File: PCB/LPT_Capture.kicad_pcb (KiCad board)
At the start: 2 copper layers, 36 x 20.8 mm, 12 parts, among them J1 USB3155-XX-X_REVA, J2 DB25 Male, U1 FT245RL

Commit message: minor routing straighten
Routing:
- net /~{TXE}: track 23.6 -> 22.9 mm
- net VCC: track 36.3 -> 35.7 mm
- net GND: vias 16 -> 15
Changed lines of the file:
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@@
   (title_block
     (title "LPT_Capture")
-    (date "2023-09-11")
-    (rev "011")
+    (date "2023-09-12")
+    (rev "012")
     (company "b.kenyon.w@gmail.com")
     (comment 1 "CC-BY-SA")
@@
     (pad "25" smd roundrect (at 15.235 -0.5 180) (size 2 4.6) (layers "B.Cu" "B.Mask") (roundrect_rratio 0.25)
       (net 1 "GND") (pinfunction "P25") (pintype "passive"))
-    (model "${KIPRJMOD}/000_LOCAL.pretty/3d/956-025-010R0.STEP"
+    (model "${KIPRJMOD}/000_LOCAL.pretty/3d/956-025-010R0.STEP" hide
       (offset (xyz 0 -9.85 -9.4))
       (scale (xyz 1 1 1))
@@
   (via (at 166.8 107.15) (size 0.5) (drill 0.3) (layers "F.Cu" "B.Cu") (free) (net 1))
   (via (at 154.7 102) (size 0.5) (drill 0.3) (layers "F.Cu" "B.Cu") (free) (net 1))
-  (via (at 144.5 102.7) (size 0.5) (drill 0.3) (layers "F.Cu" "B.Cu") (free) (net 1))
   (via (at 162.65 103.75) (size 0.5) (drill 0.3) (layers "F.Cu" "B.Cu") (net 1))
   (via (at 152.05 105.5) (size 0.5) (drill 0.3) (layers "F.Cu" "B.Cu") (free) (net 1))
@@
   (segment (start 160.5 107.25) (end 160.5 99.8) (width 0.2) (layer "F.Cu") (net 11))
   (segment (start 162.35 109.1) (end 160.5 107.25) (width 0.2) (layer "F.Cu") (net 11))
-  (segment (start 143.6 97.9) (end 142.85 97.9) (width 0.2) (layer "F.Cu") (net 12))
   (segment (start 162.9 105.225) (end 164.8 105.225) (width 0.2) (layer "F.Cu") (net 12))
+  (segment (start 142.85 98.75) (end 142.85 97.9) (width 0.2) (layer "F.Cu") (net 12))
   (via (at 162.9 105.225) (size 0.5) (drill 0.3) (layers "F.Cu" "B.Cu") (net 12))
-  (via (at 143.6 97.9) (size 0.5) (drill 0.3) (layers "F.Cu" "B.Cu") (net 12))
-  (segment (start 160.275 102.6) (end 148.3 102.6) (width 0.2) (layer "B.Cu") (net 12))
-  (segment (start 148.3 102.6) (end 143.6 97.9) (width 0.2) (layer "B.Cu") (net 12))
-  (segment (start 162.9 105.225) (end 160.275 102.6) (width 0.2) (layer "B.Cu") (net 12))
+  (via (at 142.85 98.75) (size 0.5) (drill 0.3) (layers "F.Cu" "B.Cu") (net 12))
+  (segment (start 160.275 102.6) (end 162.9 105.225) (width 0.2) (layer "B.Cu") (net 12))
+  (segment (start 142.85 98.75) (end 146.7 102.6) (width 0.2) (layer "B.Cu") (net 12))
+  (segment (start 146.7 102.6) (end 160.275 102.6) (width 0.2) (layer "B.Cu") (net 12))
   (segment (start 162.8 98.05) (end 162.8 97.9) (width 0.2) (layer "F.Cu") (net 13))
   (segment (start 163.55 98.8) (end 162.8 98.05) (width 0.2) (layer "F.Cu") (net 13))
@@
   (via (at 140.45 98.75) (size 0.5) (drill 0.3) (layers "F.Cu" "B.Cu") (net 14))
   (via (at 158.85 104.575) (size 0.5) (drill 0.3) (layers "F.Cu" "B.Cu") (net 14))
-  (segment (start 147.45 103.6) (end 147.45 102.45) (width 0.2) (layer "B.Cu") (net 14))
+  (segment (start 145.65 103.95) (end 140.45 98.75) (width 0.2) (layer "B.Cu") (net 14))
   (segment (start 158.85 104.575) (end 158.225 103.95) (width 0.2) (layer "B.Cu") (net 14))
-  (segment (start 158.225 103.95) (end 147.8 103.95) (width 0.2) (layer "B.Cu") (net 14))
-  (segment (start 147.45 102.45) (end 143.75 98.75) (width 0.2) (layer "B.Cu") (net 14))
-  (segment (start 143.75 98.75) (end 140.45 98.75) (width 0.2) (layer "B.Cu") (net 14))
-  (segment (start 147.8 103.95) (end 147.45 103.6) (width 0.2) (layer "B.Cu") (net 14))
+  (segment (start 158.225 103.95) (end 145.65 103.95) (width 0.2) (layer "B.Cu") (net 14))
   (segment (start 164.925 106.4) (end 165.9 106.4) (width 0.2) (layer "F.Cu") (net 15))
   (segment (start 155.65 105) (end 155.65 103) (width 0.6) (layer "F.Cu") (net 15))
@@
   (via (at 148.1 103.3) (size 0.5) (drill 0.3) (layers "F.Cu" "B.Cu") (net 15))
   (via (at 162.9 106.525) (size 0.5) (drill 0.3) (layers "F.Cu" "B.Cu") (net 15))
-  (segment (start 160.65 104) (end 160.65 105.05) (width 0.6) (layer "B.Cu") (net 15))
+  (segment (start 148.1 103.3) (end 158.9 103.3) (width 0.6) (layer "B.Cu") (net 15))
   (segment (start 162.125 106.525) (end 162.9 106.525) (width 0.6) (layer "B.Cu") (net 15))
-  (segment (start 159.95 103.3) (end 160.65 104) (width 0.6) (layer "B.Cu") (net 15))
-  (segment (start 160.65 105.05) (end 162.125 106.525) (width 0.6) (layer "B.Cu") (net 15))
-  (segment (start 148.1 103.3) (end 159.95 103.3) (width 0.6) (layer "B.Cu") (net 15))
+  (segment (start 158.9 103.3) (end 162.125 106.525) (width 0.6) (layer "B.Cu") (net 15))
   (segment (start 162.465 92.55) (end 159.695 92.55) (width 0.2) (layer "B.Cu") (net 16))
   (segment (start 142.85 96.1) (end 142.85 96) (width 0.2) (layer "F.Cu") (net 17))

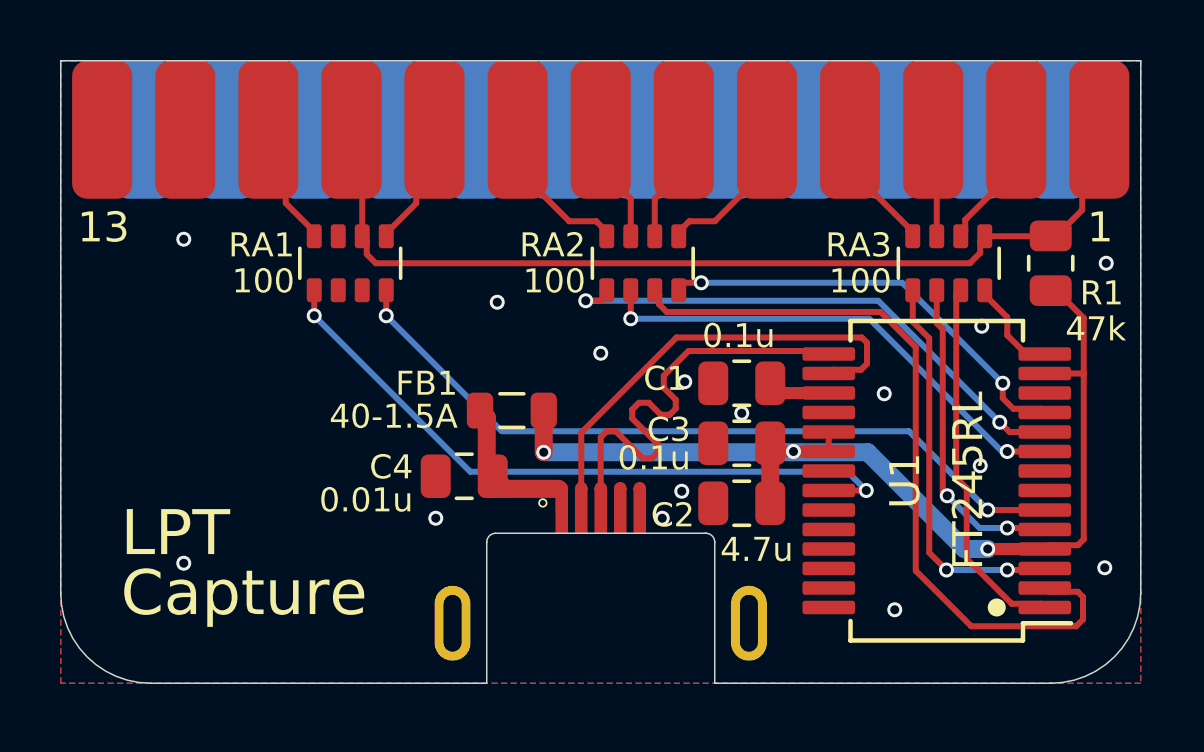
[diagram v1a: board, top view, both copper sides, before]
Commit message: add ONLINE & /RESET
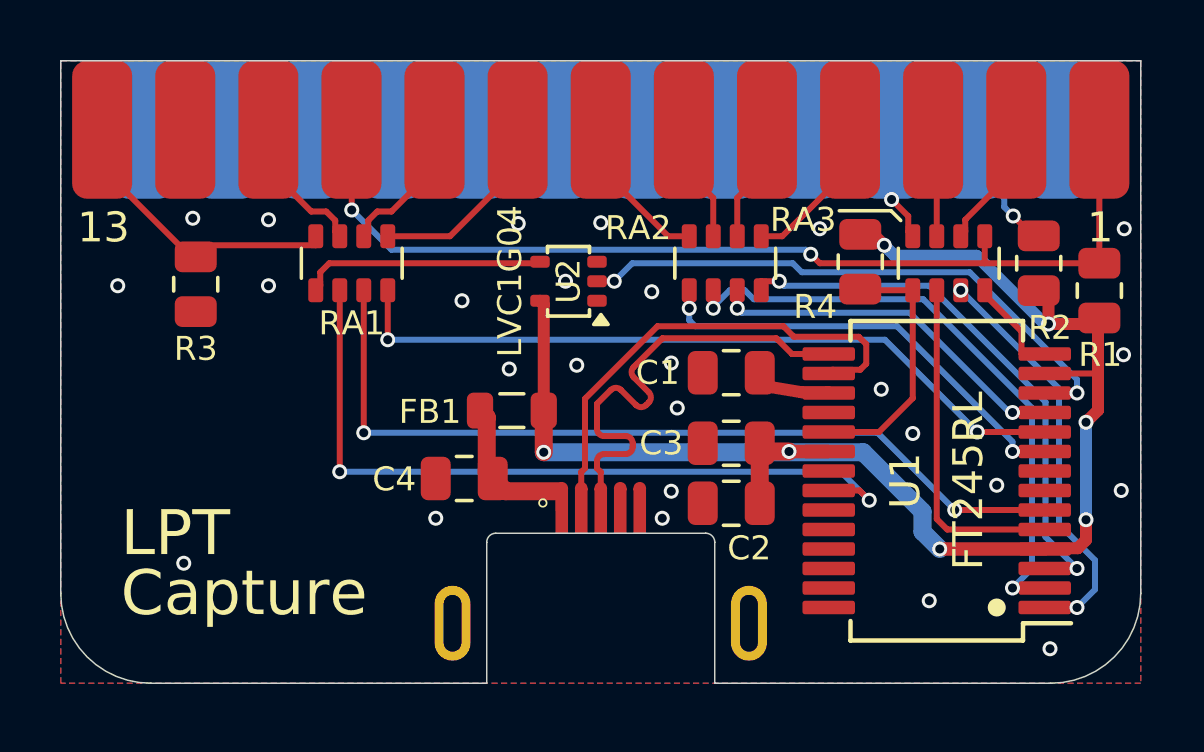
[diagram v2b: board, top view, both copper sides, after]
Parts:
- added R2: 47k, 000_LOCAL:R_0805_2012Metric, F.Cu at (164.6, 97.0)
- added R3: 47k, 000_LOCAL:R_0805_2012Metric, F.Cu at (136.5, 97.7)
- added R4: 47k, 000_LOCAL:R_0805_2012Metric, F.Cu at (158.7, 97.0)
- added U2: LVC1G04, 000_LOCAL:SOT-353_SC-70-5, F.Cu at (148.9, 97.6)
- C4: value 0.01u -> 10n
- moved RA2 2.75 mm to (154.2, 97.0)
- moved R1 1.86 mm to (166.6, 97.9)
- moved C1 0.49 mm to (154.3, 100.7)
- moved C2 0.35 mm to (154.3, 105.0)
- moved C3 0.35 mm to (154.3, 103.0)
- moved C4 0.08 mm to (145.4, 104.2)
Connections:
- net /PD0 renamed /pD0
- net /PD1 renamed /pD1
- net /~{AutoLineFeed} renamed /~{pAUTOF}
- net /~{Select-Printer} renamed /~{pSELECT}
- J2 pad 1: /~{STROBE} -> /~{pSTROBE}
- J2 pad 10: /~{STROBE} -> /~{pSTROBE}
- J2 pad 11: /BUSY -> /pBUSY
- J2 pad 13: /Select -> /pONLINE
- J2 pad 15: /RST_ERR -> /~{pERROR}
- J2 pad 16: /RST_ERR -> /~{pRESET}
- J2 pad 4: /PD2 -> /pD2
- J2 pad 5: /PD3 -> /pD3
- J2 pad 6: /PD4 -> /pD4
- J2 pad 7: /PD5 -> /pD5
- J2 pad 8: /PD6 -> /pD6
- J2 pad 9: /PD7 -> /pD7
- R1 pad 1: /~{STROBE} -> /~{pSTROBE}
- RA1 pad 1: /~{TXE} -> /PWREN
- RA1 pad 2: GND -> /~{TXE}
- RA1 pad 3: unconnected-(RA1-R3.1-Pad3) -> /D7
- RA1 pad 4: /D7 -> /D6
- RA1 pad 5: /PD7 -> /pD6
- RA1 pad 6: /~{STROBE} -> /pD7
- RA1 pad 7: GND -> /pBUSY
- RA1 pad 8: /BUSY -> /pONLINE
- RA2 pad 1: /D6 -> /D5
- RA2 pad 2: /D5 -> /D4
- RA2 pad 3: /D4 -> /D3
- RA2 pad 4: /D3 -> /D2
- RA2 pad 5: /PD3 -> /pD2
- RA2 pad 6: /PD4 -> /pD3
- RA2 pad 7: /PD5 -> /pD4
- RA2 pad 8: /PD6 -> /pD5
- RA3 pad 1: /D2 -> /~{RESET}
- RA3 pad 5: /~{STROBE} -> /~{pSTROBE}
- RA3 pad 8: /PD2 -> /~{pRESET}
- U1 pad 12: unconnected-(U1-~{PWREN}-Pad12) -> /~{PWREN}
- U1 pad 19: VCC -> /~{RESET}
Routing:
- net /~{pSTROBE}: track 0.00 -> 33.7 mm, vias 0 -> 2
- net /~{STROBE}: track 32.2 -> 0.00 mm
- net /~{PWREN}: track 0.00 -> 19.4 mm, vias 0 -> 2
- net VCC: track 35.7 -> 49.3 mm, vias 3 -> 7
- net /pONLINE: track 0.00 -> 9.76 mm
- net /~{RESET}: track 0.00 -> 8.49 mm
- net /PWREN: track 0.00 -> 8.13 mm
- net /D6: track 18.0 -> 24.8 mm
- net /pD6: track 0.00 -> 6.56 mm
- net /D2: track 13.1 -> 18.5 mm
- net /PD6: track 5.31 -> 0.00 mm
- net /PD3: track 5.27 -> 0.00 mm
- net /D4: track 25.7 -> 20.5 mm, vias 0 -> 2
- net /pD2: track 0.00 -> 5.19 mm
- net /pD5: track 0.00 -> 5.18 mm
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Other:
- board text added: "R1-R4 ${00000000-0000-0000-0000-000060bbe2fe:VALUE} RA1-RA3 ${00000000-0000-0000-0000-000060bbe78d:VALUE} C1,C3 ${00000000-0000-0000-0000-000060bbeb15:VALUE} C2 ${00000000-0000-0000-0000-000060bbe5e0:VALUE} C4 ${00000000-0000-0000-0000-000060cac7fa:VALUE} FB1 ${00000000-0000-0000-0000-000060ca1001:VALUE}"

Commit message: pfet invert for online, bom
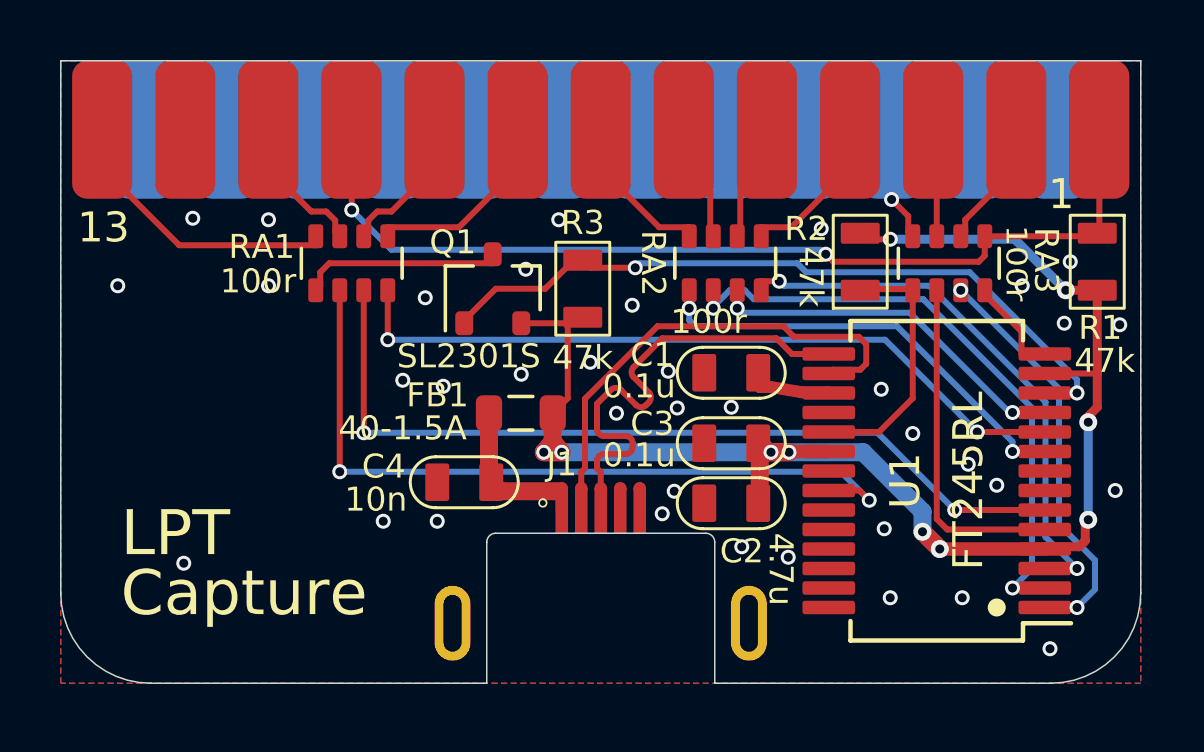
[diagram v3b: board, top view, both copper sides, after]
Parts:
- removed the R2 at (164.6, 97.0)
- removed U2: LVC1G04, 000_LOCAL:SOT-353_SC-70-5
- added N1: Housing, 000_LOCAL:DSUB-25_Housing, F.Cu at (150.0, 92.5)
- added Q1: SL2301S, 000_LOCAL:SOT-23, F.Cu at (146.4, 97.8)
- C1, C2, C3, C4: footprint 000_LOCAL:C_0805_2012Metric -> 000_LOCAL:C_0805
- J1: value USB3155-XX-X_REVA -> USB3155-XX-X; footprint 000_LOCAL:GCT_USB3155-XX-X_REVA -> 000_LOCAL:GCT_USB3155-XX-X
- R1, R3: footprint 000_LOCAL:R_0805_2012Metric -> 000_LOCAL:R_0805
- R2: renamed from R4; footprint 000_LOCAL:R_0805_2012Metric -> 000_LOCAL:R_0805
- RA1, RA2, RA3: value 100 -> 100r
- moved R3 12.9 mm to (149.4, 97.8), turned to -90 degrees
- moved J2 1.90 mm to (150.0, 90.2)
- moved R1 0.97 mm to (166.6, 97.0)
- moved FB1 0.31 mm to (147.3, 102.0)
- moved C4 0.12 mm to (145.4, 104.3)
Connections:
- R3 pad 1: GND -> /~{PWREN}
- R3 pad 2: /pONLINE -> VCC
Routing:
- net /~{PWREN}: track 19.4 -> 24.6 mm
- net /~{pERROR}: track 4.53 -> 0.00 mm, vias 1 -> 0
- net /~{pRESET}: track 1.52 -> 3.84 mm
- net VCC: track 49.3 -> 51.0 mm, vias 7 -> 10
- net /PWREN: track 8.13 -> 6.84 mm
- net /~{pSTROBE}: track 33.7 -> 32.5 mm
- net GND: vias 26 -> 37
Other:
- board text added: "J1: ${00000000-0000-0000-0000-000060db353c:VALUE}"
- board text added: "PCB THICKNESS 1.2mm"
- board text removed: "R1-R4 ${00000000-0000-0000-0000-000060bbe2fe:VALUE} RA1-RA3 ${00000000-0000-0000-0000-000060bbe78d:VALUE} C1,C3 ${00000000-0000-0000-0000-000060bbeb15:VALUE} C2 ${00000000-0000-0000-0000-000060bbe5e0:VALUE} C4 ${00000000-0000-0000-0000-000060cac7fa:VALUE} FB1 ${00000000-0000-0000-0000-000060ca1001:VALUE}"

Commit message: add /SELECT
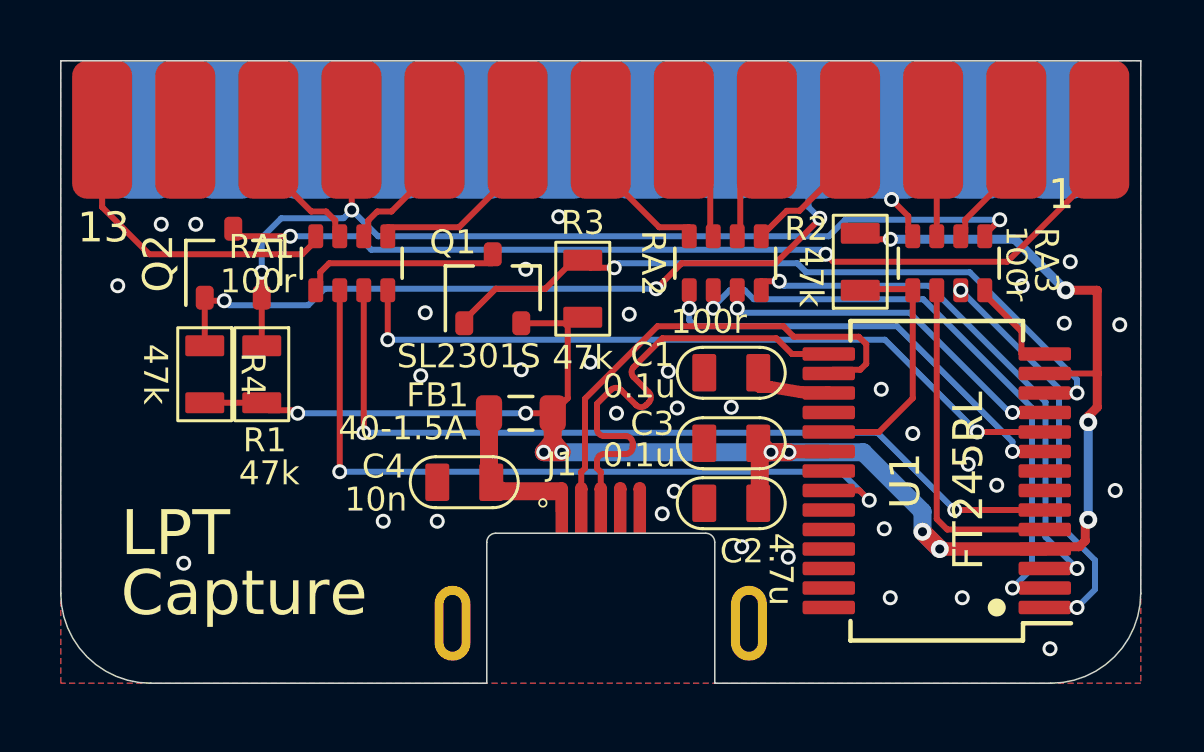
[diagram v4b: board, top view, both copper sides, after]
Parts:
- added Q2: SL2301S, 000_LOCAL:SOT-23, F.Cu at (137.8, 97.0)
- added R4: 47k, 000_LOCAL:R_0805, F.Cu at (136.8, 100.7)
- moved R1 28.1 mm to (138.7, 100.7)
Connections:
- J2 pad 10: /~{pSTROBE} -> /~{STROBE}
- R1 pad 1: /~{pSTROBE} -> /~{STROBE}
- RA3 pad 5: /~{pSTROBE} -> /~{STROBE}
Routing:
- net /~{STROBE}: track 0.00 -> 32.6 mm, vias 0 -> 3
- net /~{pSELECT}: track 0.00 -> 26.6 mm, vias 0 -> 3
- net VCC: track 51.0 -> 62.8 mm, vias 10 -> 12
- net /pONLINE: track 9.76 -> 10.7 mm
- net /~{pSTROBE}: track 32.5 -> 31.9 mm
- net GND: vias 37 -> 34

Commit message: silkscreen
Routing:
- net VCC: track 62.8 -> 62.2 mm

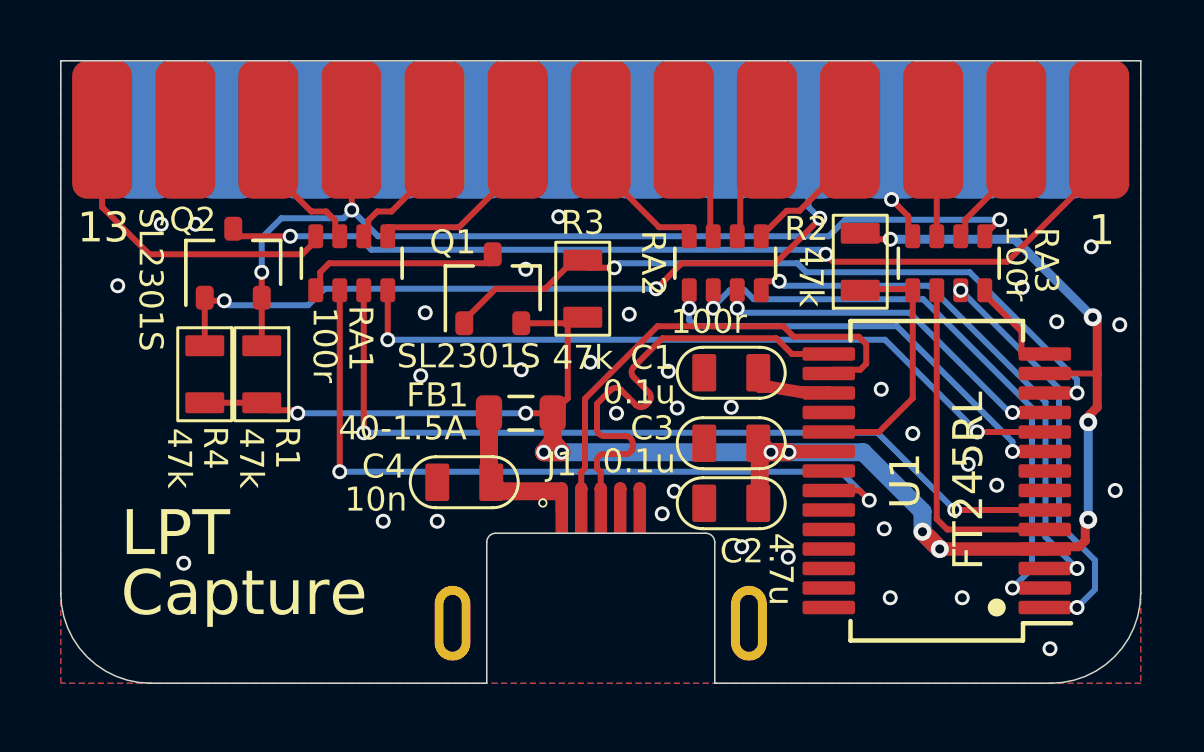
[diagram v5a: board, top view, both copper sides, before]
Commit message: pulldown /SELIN
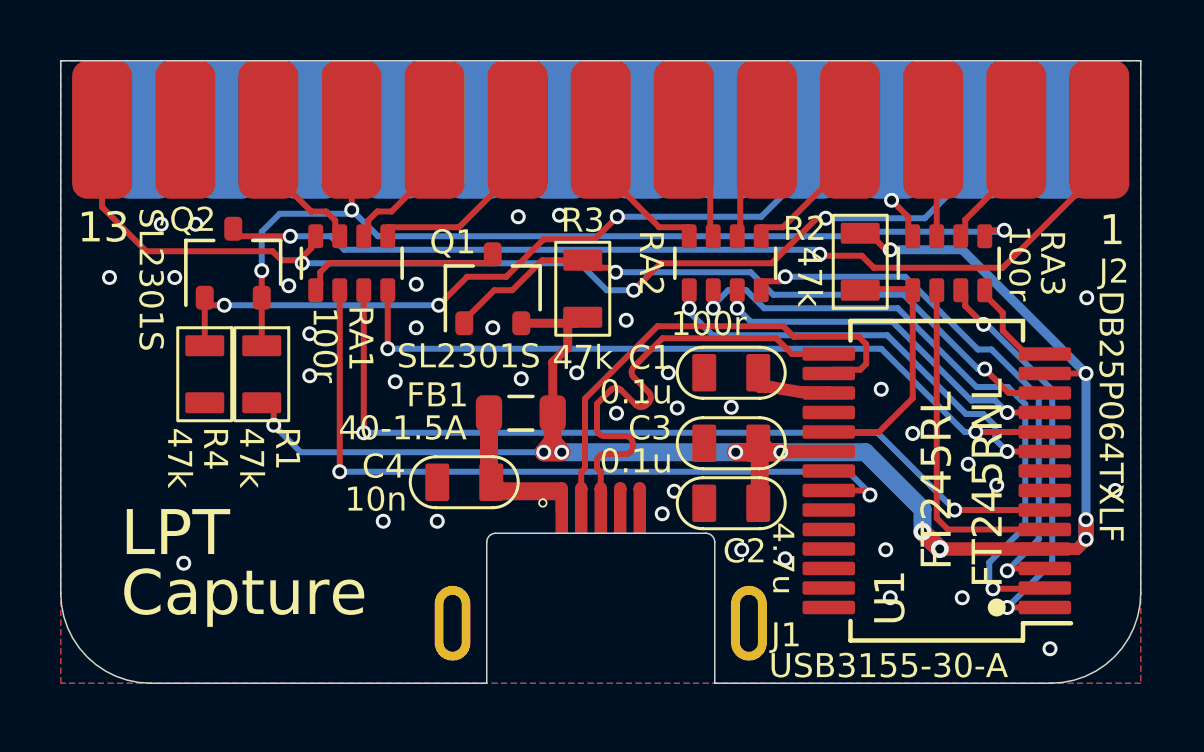
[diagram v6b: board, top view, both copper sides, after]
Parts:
- J1: value USB3155-XX-X -> USB3155-30-A
- J2: value DB25 Male -> DB25P064TXLF
- N1: value Housing -> MHCCOV-25-SN-LG
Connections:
- net /PWREN renamed /ONLINE
- net /~{pSELECT} renamed /~{pSELIN}
- J2 pad 15: /~{pERROR} -> /pONLINE
- R4 pad 2: VCC -> GND
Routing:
- net /pONLINE: track 10.7 -> 36.9 mm, vias 0 -> 3
- net GND: track 0.00 -> 20.7 mm, vias 34 -> 37
- net /~{PWREN}: track 24.6 -> 22.1 mm
- net VCC: track 62.2 -> 60.6 mm, vias 12 -> 11
- net /~{pSELIN}: track 26.6 -> 25.2 mm
- net /D4: track 20.5 -> 21.3 mm
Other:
- board text added: "BACKSHELL: ${e31e62e7-9523-48c9-88c9-8276f3149c83:VALUE}"
- board text removed: "J1: ${00000000-0000-0000-0000-000060db353c:VALUE}"
- board text removed: "PCB THICKNESS 1.2mm"
